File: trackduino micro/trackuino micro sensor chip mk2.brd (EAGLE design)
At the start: 49.8 x 19 mm, 41 parts, among them IC2 74AHC1G125DBV, SW1 SPST_TACT-KMR2, U1 ATMEGA168MLF, Y1 16MHZ

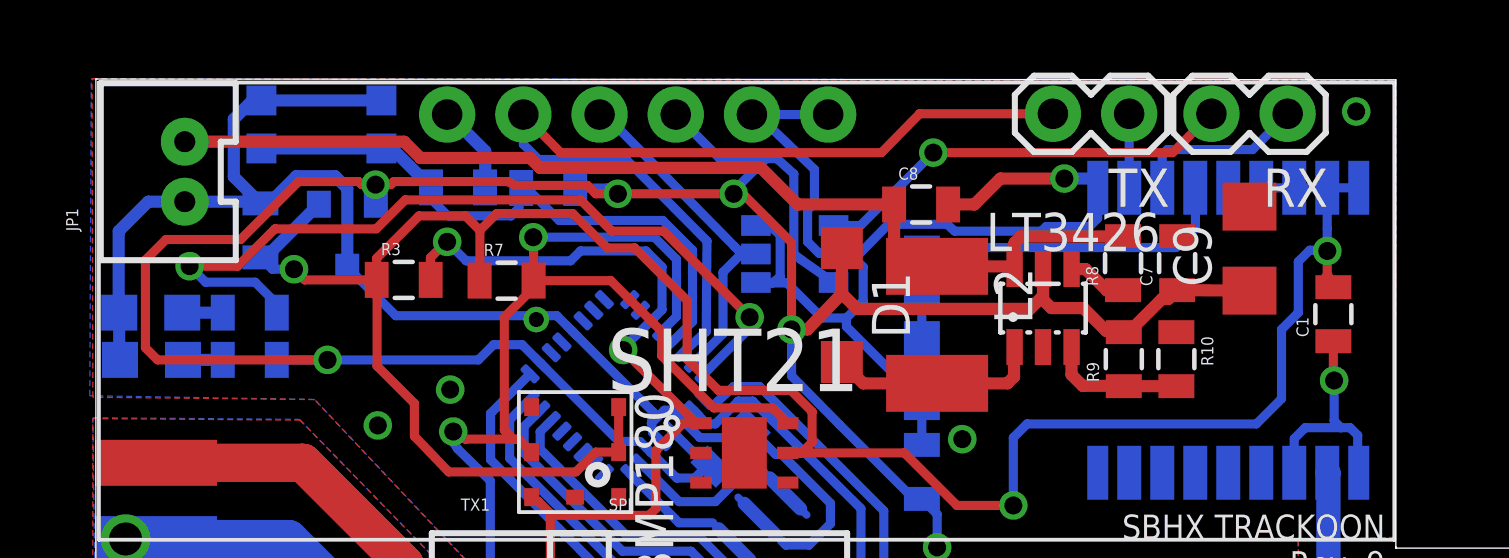
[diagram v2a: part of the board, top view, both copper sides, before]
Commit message: tx rx 2mm headers
replaced .1” serial headers on chip and non chip version with 2mm
headers
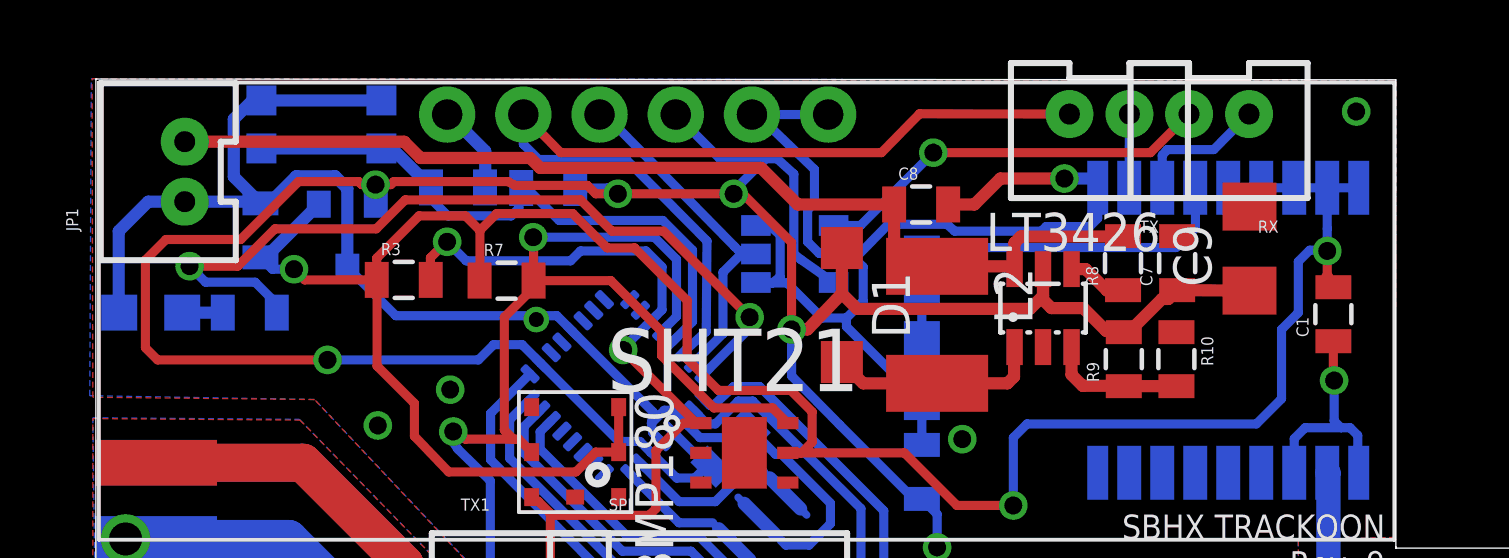
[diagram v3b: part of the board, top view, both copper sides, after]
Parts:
- removed R4: 330ohm, SparkFun-Resistors:0805
- removed VCC: (no value), adafruit:CHIP-LED0805
- RX, TX: device SparkFun-Connectors:1X02 -> SparkFun-Connectors:JST-2-PTH-VERT
- moved RX 2.35 mm to (37.4, 17.3)
- moved TX 1.14 mm to (33.5, 17.3)
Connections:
- removed net N$8: R4.1, VCC.A
- net GND: no longer VCC.C
- net VCC: no longer R4.2
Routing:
- net VCC: track 99.2 -> 97.5 mm
- net GND: track 123.3 -> 121.7 mm
- net N$8: track 1.33 -> 0.00 mm
- net RX1: track 5.85 -> 4.56 mm
- net TX1: track 14.1 -> 13.4 mm
- net RXO: track 31.3 -> 31.8 mm
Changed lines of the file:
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@@
 <element name="C3" library="SparkFun-Capacitors" package="0805" value=".1uf" x="21.1582" y="6.7564" rot="MR315"/>
 <element name="C4" library="SparkFun-Capacitors" package="0805" value=".1uf" x="27.5336" y="5.9436" rot="MR270"/>
-<element name="VCC" library="adafruit" package="CHIP-LED0805" value="" x="1.8542" y="9.6774" rot="MR270"/>
-<element name="R4" library="SparkFun-Resistors" package="0805" value="330ohm" x="5.1308" y="9.6774" rot="MR180"/>
 <element name="FTDI" library="SparkFun-Connectors" package="1X06_NO_SILK" value="" x="11.7094" y="17.8562" rot="MR180">
 <attribute name="PROD_ID" value="CONN-08437" x="11.7094" y="17.8562" size="1.778" layer="28" rot="MR180" display="off"/>
@@
 <element name="R5" library="SparkFun-Resistors" package="0805" value="10k" x="15.077075" y="15.407278125" rot="MR180"/>
 <element name="C5" library="SparkFun-Capacitors" package="0805" value=".1uf" x="12.071159375" y="15.427575" rot="MR0"/>
-<element name="TX" library="SparkFun-Connectors" package="1X02" value="TX" x="34.4424" y="17.8816" rot="R180"/>
+<element name="TX" library="SparkFun-Connectors" package="JST-2-PTH-VERT" value="TX" x="33.4518" y="17.3228" rot="R180"/>
 <element name="SPI" library="SparkFun-Connectors" package="JST-4-PTH-VERT" value="" x="20.0914" y="1.651"/>
 <element name="FRAME1" library="SparkFun-Aesthetics" package="CREATIVE_COMMONS" value="FRAME-LETTER" x="14.3764" y="-8.1534"/>
@@
 <element name="U$1" library="Ava" package="UBLOX_MAX" value="UBLOX_MAX" x="37.7952" y="10.4648" rot="MR90"/>
 <element name="SW1" library="adafruit" package="KMR2" value="SPST_TACT-KMR2" x="7.5184" y="17.526" rot="MR180"/>
-<element name="RX" library="SparkFun-Connectors" package="1X02" value="RX" x="39.7256" y="17.8816" rot="R180"/>
+<element name="RX" library="SparkFun-Connectors" package="JST-2-PTH-VERT" value="RX" x="37.4396" y="17.3228" rot="R180"/>
 <element name="BMP180" library="SparkFun-Sensors" package="BMP180" value="BMP180" x="15.9766" y="6.604" rot="R270"/>
 <element name="R3" library="SparkFun-Resistors" package="0805" value="4.7k" x="10.2616" y="12.3444"/>
@@
 <contactref element="C3" pad="1"/>
 <contactref element="C4" pad="1"/>
-<contactref element="VCC" pad="C"/>
 <contactref element="U1" pad="3"/>
 <contactref element="U1" pad="5"/>
@@
 <wire x1="0.762" y1="13.97" x2="0.762" y2="11.269" width="0.4064" layer="16"/>
 <wire x1="0.762" y1="11.269" x2="0.7788" y2="11.2522" width="0.4064" layer="16"/>
-<wire x1="0.7788" y1="11.2522" x2="0.7788" y2="9.7028" width="0.4064" layer="16"/>
-<wire x1="0.7788" y1="9.7028" x2="0.8042" y2="9.6774" width="0.4064" layer="16"/>
 <wire x1="2.963" y1="14.9512" x2="5.4306" y2="14.9512" width="0.4064" layer="16"/>
 <wire x1="5.4306" y1="14.9512" x2="5.4864" y2="14.8954" width="0.4064" layer="16"/>
@@
 <contactref element="C3" pad="2"/>
 <contactref element="C4" pad="2"/>
-<contactref element="R4" pad="2"/>
 <contactref element="U1" pad="4"/>
 <contactref element="U1" pad="6"/>
@@
 <wire x1="13.2588" y1="10.1854" x2="12.7508" y2="9.6774" width="0.3048" layer="16"/>
 <wire x1="12.7508" y1="9.6774" x2="7.7216" y2="9.6774" width="0.3048" layer="16"/>
-<wire x1="7.7216" y1="9.6774" x2="6.0308" y2="9.6774" width="0.3048" layer="16"/>
 <wire x1="14.828015625" y1="9.566215625" x2="17.43463125" y2="6.9596" width="0.3048" layer="16"/>
 <wire x1="17.43463125" y1="6.9596" x2="18.1356" y2="6.9596" width="0.3048" layer="16"/>
@@
 <wire x1="27.5336" y1="11.6222" x2="27.5336" y2="10.3718" width="0.3048" layer="16"/>
 </signal>
-<signal name="N$8">
-<contactref element="VCC" pad="A"/>
-<contactref element="R4" pad="1"/>
-<wire x1="2.9042" y1="9.6774" x2="4.2308" y2="9.6774" width="0.4064" layer="16"/>
-</signal>
 <signal name="DTR">
 <contactref element="FTDI" pad="1"/>
@@
 <wire x1="14.2494" y1="16.8656" x2="14.2494" y2="17.8562" width="0.3048" layer="16"/>
 <contactref element="TX" pad="2"/>
-<wire x1="31.9024" y1="17.8816" x2="27.4574" y2="17.8816" width="0.3048" layer="1"/>
+<wire x1="32.4518" y1="17.8728" x2="27.4574" y2="17.8816" width="0.3048" layer="1"/>
 <wire x1="27.4574" y1="17.8816" x2="26.1874" y2="16.5862" width="0.3048" layer="1"/>
 <wire x1="26.1874" y1="16.5862" x2="15.494" y2="16.5862" width="0.3048" layer="1"/>
@@
 <wire x1="25.4864" y1="14.158" x2="27.9146" y2="16.5862" width="0.3048" layer="16"/>
 <via x="27.9146" y="16.5862" extent="1-16" drill="0.6" shape="square"/>
-<wire x1="27.9146" y1="16.5862" x2="35.8902" y2="16.5862" width="0.3048" layer="1"/>
-<wire x1="35.8902" y1="16.5862" x2="37.1856" y2="17.8816" width="0.3048" layer="1"/>
+<wire x1="27.9146" y1="16.5862" x2="35.1536" y2="16.5862" width="0.3048" layer="1"/>
+<wire x1="35.1536" y1="16.5862" x2="36.4396" y2="17.8728" width="0.3048" layer="1"/>
 </signal>
 <signal name="VDDD">
@@
 <wire x1="35.5452" y1="15.4148" x2="35.5452" y2="16.4952" width="0.3048" layer="16"/>
 <wire x1="35.5452" y1="16.4952" x2="35.7124" y2="16.6878" width="0.3048" layer="16"/>
-<wire x1="35.7124" y1="16.6878" x2="38.5572" y2="16.6878" width="0.3048" layer="16"/>
-<wire x1="38.5572" y1="16.6878" x2="39.7256" y2="17.8816" width="0.3048" layer="16"/>
+<wire x1="35.7124" y1="16.6878" x2="37.2618" y2="16.6878" width="0.3048" layer="16"/>
+<wire x1="37.2618" y1="16.6878" x2="38.4396" y2="17.8728" width="0.3048" layer="16"/>
 </signal>
 <signal name="TX">
 <contactref element="U$1" pad="2_TXD1"/>
 <contactref element="TX" pad="1"/>
-<wire x1="34.4424" y1="17.8816" x2="34.4424" y2="15.4176" width="0.3048" layer="16"/>
+<wire x1="34.4518" y1="17.8728" x2="34.4424" y2="15.4176" width="0.3048" layer="16"/>
 <wire x1="34.4424" y1="15.4176" x2="34.4452" y2="15.4148" width="0.3048" layer="16"/>
 </signal>

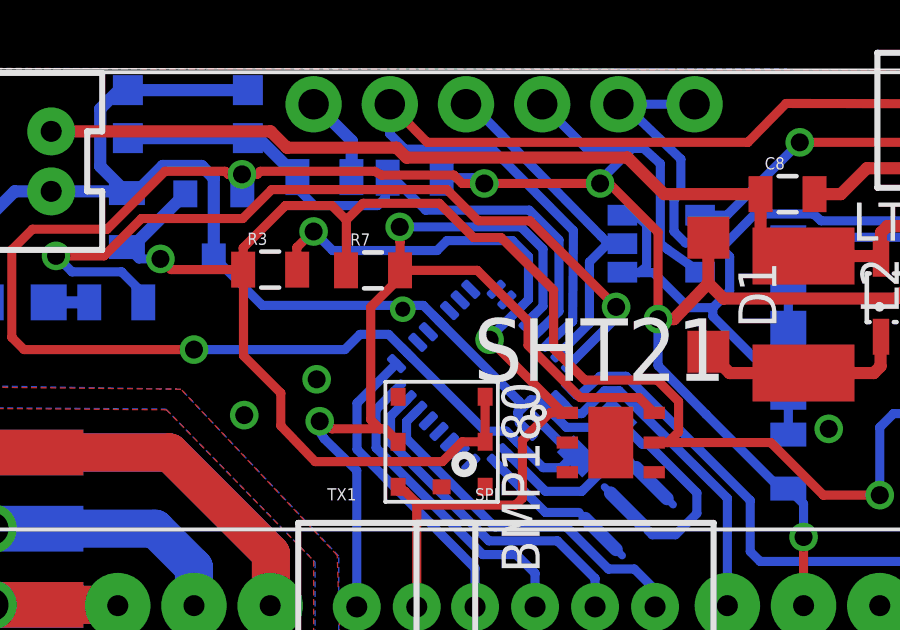
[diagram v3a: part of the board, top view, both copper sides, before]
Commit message: Removed Via From Under MCU
Removed a via from under the ATMEGA328P to prevent any potential
shorts.
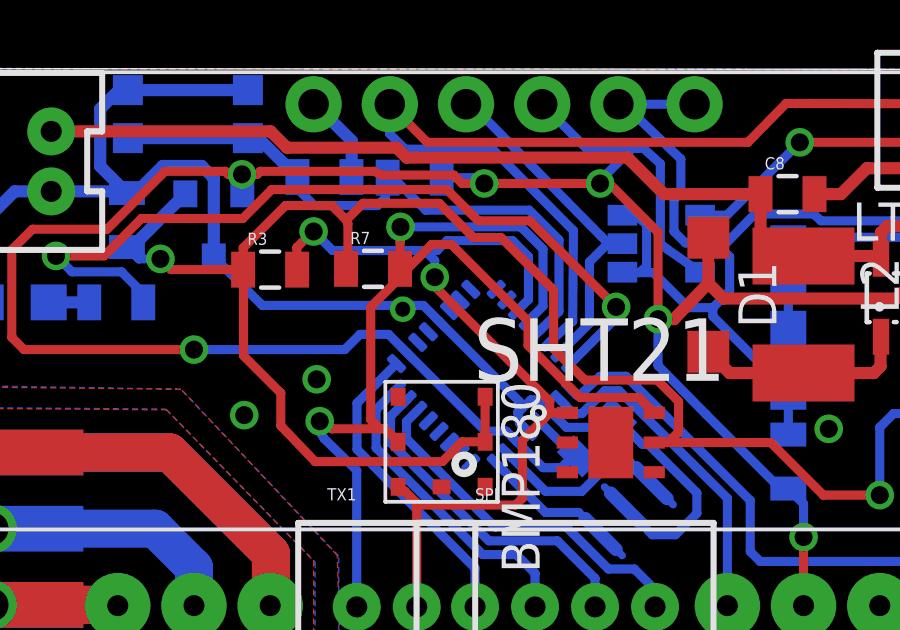
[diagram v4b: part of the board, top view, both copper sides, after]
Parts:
- moved R7 0.05 mm to (13.7, 12.4)
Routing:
- net SDA: track 28.0 -> 30.1 mm
- net SCL: track 35.5 -> 36.2 mm
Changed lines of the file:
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@@
 <?xml version="1.0" encoding="utf-8"?>
 <!DOCTYPE eagle SYSTEM "eagle.dtd">
-<eagle version="7.2.0">
+<eagle version="7.1.0">
 <drawing>
 <settings>
@@
 <element name="BMP180" library="SparkFun-Sensors" package="BMP180" value="BMP180" x="15.9766" y="6.604" rot="R270"/>
 <element name="R3" library="SparkFun-Resistors" package="0805" value="4.7k" x="10.2616" y="12.3444"/>
-<element name="R7" library="SparkFun-Resistors" package="0805" value="4.7k" x="13.6906" y="12.319"/>
+<element name="R7" library="SparkFun-Resistors" package="0805" value="4.7k" x="13.6906" y="12.3698"/>
 <element name="LT3426" library="adafruit" package="SOT23-6" value="LT3426" x="31.5722" y="11.4046"/>
 <element name="D1" library="diode" package="SOD123" value="MBR120VLSFT1" x="24.8666" y="11.5062" rot="R270"/>
@@
 <wire x1="10.7696" y1="14.478" x2="12.319" y2="14.478" width="0.3048" layer="1"/>
 <wire x1="12.319" y1="14.478" x2="12.8016" y2="13.9954" width="0.3048" layer="1"/>
-<wire x1="12.8016" y1="13.9954" x2="12.8016" y2="12.33" width="0.3048" layer="1"/>
-<wire x1="12.8016" y1="12.33" x2="12.7906" y2="12.319" width="0.3048" layer="1"/>
-<wire x1="12.7906" y1="12.319" x2="12.7906" y2="12.203" width="0.3048" layer="1"/>
+<wire x1="12.8016" y1="13.9954" x2="12.8524" y2="13.8794" width="0.3048" layer="1"/>
 <wire x1="19.7104" y1="11.6586" x2="17.9578" y2="13.4112" width="0.3048" layer="1"/>
 <wire x1="17.9578" y1="13.4112" x2="17.0434" y2="13.4112" width="0.3048" layer="1"/>
@@
 <wire x1="40.4622" y1="13.335" x2="41.021" y2="13.335" width="0.3048" layer="16"/>
 <wire x1="41.021" y1="13.335" x2="41.0464" y2="13.3096" width="0.3048" layer="16"/>
+<wire x1="12.8524" y1="13.8794" x2="12.8524" y2="12.4316" width="0.3048" layer="1"/>
+<wire x1="12.8524" y1="12.4316" x2="12.7906" y2="12.3698" width="0.3048" layer="1"/>
 </signal>
 <signal name="N$1">
@@
 <wire x1="18.3388" y1="13.3096" x2="16.1544" y2="13.3096" width="0.3048" layer="16"/>
 <wire x1="16.1544" y1="13.3096" x2="15.8242" y2="12.9794" width="0.3048" layer="16"/>
-<wire x1="15.8242" y1="12.9794" x2="12.3444" y2="12.9794" width="0.3048" layer="16"/>
+<wire x1="15.8242" y1="12.9794" x2="15.4178" y2="12.9794" width="0.3048" layer="16"/>
+<wire x1="15.4178" y1="12.9794" x2="12.3444" y2="12.9794" width="0.3048" layer="16"/>
 <wire x1="12.3444" y1="12.9794" x2="11.7094" y2="13.6144" width="0.3048" layer="16"/>
 <via x="11.7094" y="13.6144" extent="1-16" drill="0.6" shape="square"/>
@@
 <wire x1="18.669" y1="6.6548" x2="19.5834" y2="7.5692" width="0.3048" layer="1"/>
 <wire x1="19.5834" y1="7.5692" x2="20.1676" y2="7.5692" width="0.3048" layer="1"/>
-<wire x1="20.1676" y1="7.5692" x2="20.0152" y2="7.5692" width="0.3048" layer="1"/>
-<wire x1="20.0152" y1="7.5692" x2="17.5768" y2="10.0076" width="0.3048" layer="1"/>
-<via x="17.5768" y="10.0076" extent="1-16" drill="0.6"/>
-<wire x1="17.5768" y1="10.0076" x2="17.5768" y2="10.07765625" width="0.3048" layer="16"/>
-<wire x1="17.5768" y1="10.07765625" x2="18.504971875" y2="10.980428125" width="0.3048" layer="16"/>
 <contactref element="TX1" pad="2"/>
 <wire x1="15.1478" y1="1.101" x2="15.1478" y2="4.5626" width="0.3048" layer="1"/>
 <wire x1="15.1478" y1="4.5626" x2="14.7552" y2="4.9552" width="0.3048" layer="1"/>
+<wire x1="19.5834" y1="7.5692" x2="19.5834" y2="7.9502" width="0.3048" layer="1"/>
+<wire x1="19.5834" y1="7.9502" x2="15.748" y2="11.7856" width="0.3048" layer="1"/>
+<wire x1="15.748" y1="11.7856" x2="15.748" y2="12.0904" width="0.3048" layer="1"/>
+<via x="15.748" y="12.0904" extent="1-16" drill="0.6"/>
+<wire x1="15.748" y1="12.0904" x2="15.748" y2="12.6492" width="0.3048" layer="16"/>
+<wire x1="15.748" y1="12.6492" x2="15.4178" y2="12.9794" width="0.3048" layer="16"/>
 </signal>
 <signal name="SCL">
@@
 <wire x1="19.3548" y1="11.12315" x2="19.3548" y2="13.0302" width="0.3048" layer="16"/>
 <wire x1="19.3548" y1="13.0302" x2="18.6182" y2="13.7668" width="0.3048" layer="16"/>
-<wire x1="14.5906" y1="12.319" x2="14.5906" y2="13.2698" width="0.3048" layer="1"/>
-<wire x1="14.5906" y1="13.2698" x2="14.5796" y2="13.7668" width="0.3048" layer="1"/>
-<via x="14.5796" y="13.7668" extent="1-16" drill="0.6" shape="square"/>
-<wire x1="14.5796" y1="13.7668" x2="18.6182" y2="13.7668" width="0.3048" layer="16"/>
+<wire x1="14.5906" y1="12.3698" x2="14.5906" y2="13.2698" width="0.3048" layer="1"/>
+<wire x1="14.5906" y1="13.2698" x2="14.605" y2="13.7668" width="0.3048" layer="1"/>
+<via x="14.605" y="13.7668" extent="1-16" drill="0.6" shape="square"/>
+<wire x1="14.605" y1="13.7668" x2="18.6182" y2="13.7668" width="0.3048" layer="16"/>
 <contactref element="SHT21" pad="6"/>
 <wire x1="23.0632" y1="7.5692" x2="22.5552" y2="8.0772" width="0.3048" layer="1"/>
@@
 <wire x1="20.5994" y1="8.0772" x2="18.858525" y2="9.818075" width="0.3048" layer="1"/>
 <wire x1="18.858525" y1="9.818075" x2="18.858525" y2="10.626875" width="0.3048" layer="1"/>
-<wire x1="18.858525" y1="10.626875" x2="17.1664" y2="12.319" width="0.3048" layer="1"/>
-<wire x1="17.1664" y1="12.319" x2="14.5906" y2="12.319" width="0.3048" layer="1"/>
+<wire x1="18.858525" y1="10.626875" x2="16.3028" y2="13.1826" width="0.3048" layer="1"/>
+<wire x1="16.3028" y1="13.1826" x2="15.6464" y2="13.1826" width="0.3048" layer="1"/>
+<wire x1="15.6464" y1="13.1826" x2="14.8336" y2="12.3698" width="0.3048" layer="1"/>
+<wire x1="14.8336" y1="12.3698" x2="14.5906" y2="12.3698" width="0.3048" layer="1"/>
 <contactref element="TX1" pad="1"/>
 <wire x1="13.1478" y1="1.101" x2="13.1478" y2="5.6482" width="0.3048" layer="16"/>
@@
 <wire x1="13.9192" y1="7.0358" x2="14.0948" y2="7.0358" width="0.3048" layer="1"/>
 <wire x1="14.0948" y1="7.0358" x2="14.5266" y2="6.604" width="0.3048" layer="1"/>
-<wire x1="14.5906" y1="12.319" x2="14.5906" y2="12.076" width="0.3048" layer="1"/>
-<wire x1="14.5906" y1="12.076" x2="13.6144" y2="11.0998" width="0.3048" layer="1"/>
+<wire x1="14.5906" y1="12.3698" x2="14.6668" y2="12.1522" width="0.3048" layer="1"/>
+<wire x1="14.6668" y1="12.1522" x2="13.6144" y2="11.0998" width="0.3048" layer="1"/>
 <wire x1="13.6144" y1="11.0998" x2="13.6144" y2="7.3406" width="0.3048" layer="1"/>
 <wire x1="13.6144" y1="7.3406" x2="13.9192" y2="7.0358" width="0.3048" layer="1"/>

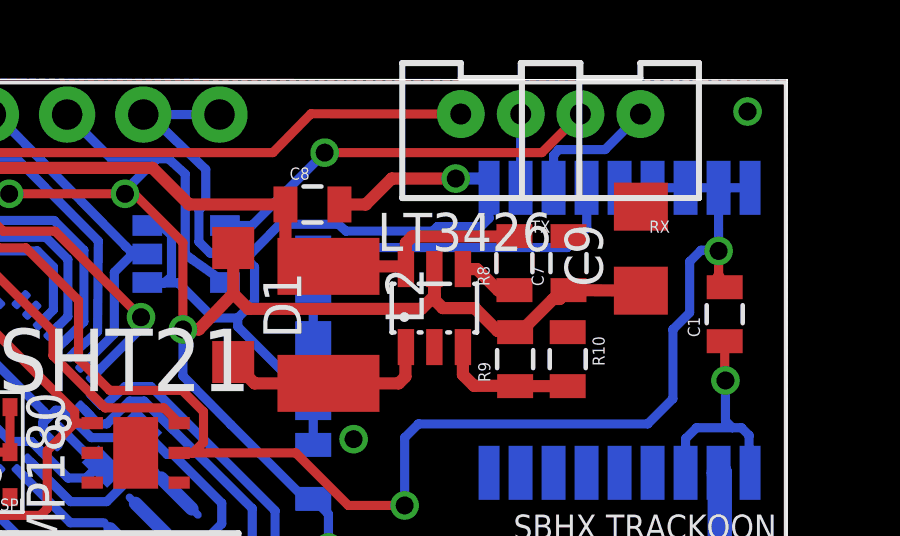
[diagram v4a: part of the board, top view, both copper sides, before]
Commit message: Standardized round via
Changed all via on production boards to round, and moved hidden via on
solar board out from under the atmega. Also fixed bom to specify
max-m8q gps.
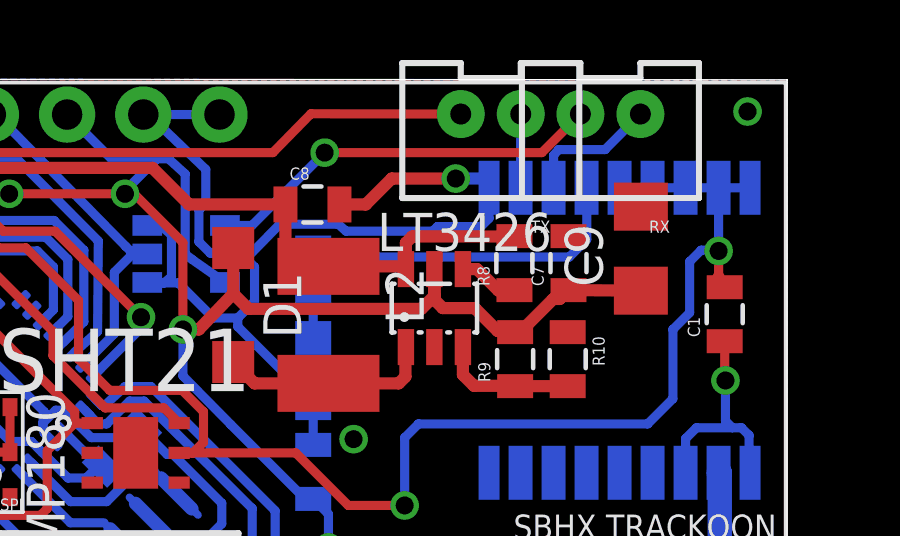
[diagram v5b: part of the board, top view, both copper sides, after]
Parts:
- renumbered LED1 to GPSLOCK
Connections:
- net N$2 renamed PPS
